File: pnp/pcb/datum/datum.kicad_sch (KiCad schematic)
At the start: 5 parts

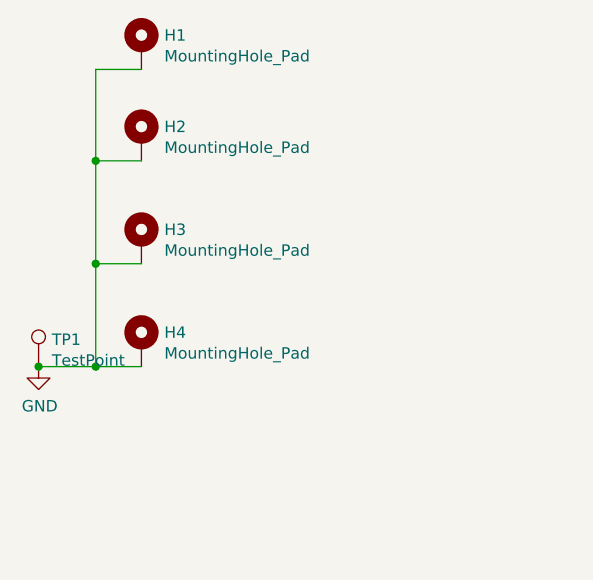
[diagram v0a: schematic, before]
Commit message: add missing component which was on the PCB but not on the schematic
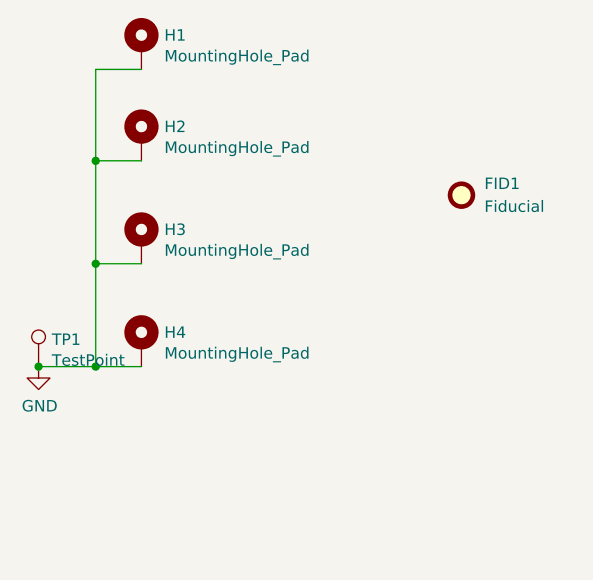
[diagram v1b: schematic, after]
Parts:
- added FID1: Fiducial, Fiducial:Fiducial_1mm_Mask2mm, symbol Mechanical:Fiducial
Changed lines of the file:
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@@
+		)
+	)
+	(symbol
+		(lib_id "Mechanical:Fiducial")
+		(at 118.11 85.09 0)
+		(unit 1)
+		(exclude_from_sim yes)
+		(in_bom no)
+		(on_board yes)
+		(dnp no)
+		(fields_autoplaced yes)
+		(property "Reference" "FID1"
+			(at 120.65 83.8199 0)
+			(effects
+				(font
+					(size 1.27 1.27)
+				)
+				(justify left)
+			)
+		)
+		(property "Value" "Fiducial"
+			(at 120.65 86.3599 0)
+			(effects
+				(font
+					(size 1.27 1.27)
+				)
+				(justify left)
+			)
+		)
+		(property "Footprint" "Fiducial:Fiducial_1mm_Mask2mm"
+			(at 118.11 85.09 0)
+			(effects
+				(font
+					(size 1.27 1.27)
+				)
+				(hide yes)
+			)
+		)
+		(property "Datasheet" "~"
+			(at 118.11 85.09 0)
+			(effects
+				(font
+					(size 1.27 1.27)
+				)
+				(hide yes)
+			)
+		)
+		(property "Description" "Fiducial Marker"
+			(at 118.11 85.09 0)
+			(effects
+				(font
+					(size 1.27 1.27)
+				)
+				(hide yes)
+			)
+		)
+		(instances
+			(project "datum"
+				(path "/e63e39d7-6ac0-4ffd-8aa3-1841a4541b55"
+					(reference "FID1")
+					(unit 1)
+				)
+			)
 		)
 	)

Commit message: Fix fiducial reference designators
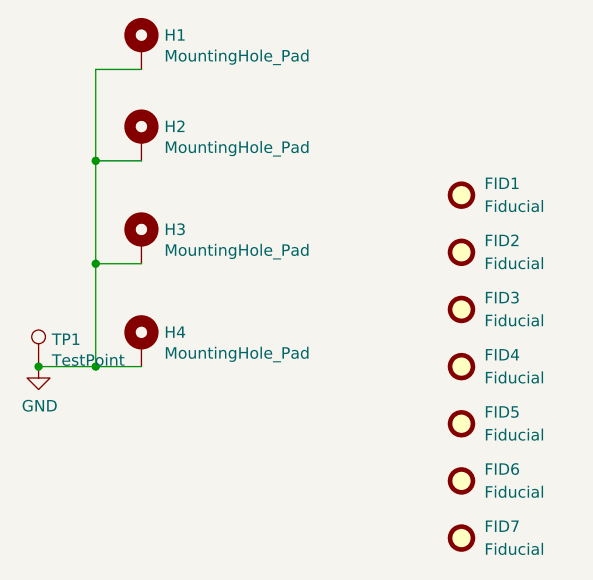
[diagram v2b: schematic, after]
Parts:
- added FID2, FID3, FID4, FID5, FID6, FID7: Fiducial, Fiducial:Fiducial_1mm_Mask3mm, symbol Mechanical:Fiducial
